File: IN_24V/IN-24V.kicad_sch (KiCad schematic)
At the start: 12 parts, among them U1 SN74LVC1T45DCK

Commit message: IN-24V
correction cartouche
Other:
- company: Style And Design -> (none)
- title: Module OUT 1 5V -> IN 24V
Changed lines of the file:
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@@
 	(paper "A4")
 	(title_block
-		(title "Module OUT 1 5V")
-		(date "2024-03-04")
-		(rev "00")
-		(company "Style And Design")
-		(comment 1 "T.ORLANDI")
+		(title "IN 24V")
+		(date "2024-12-03")
+		(rev "0")
 	)
 	(junction

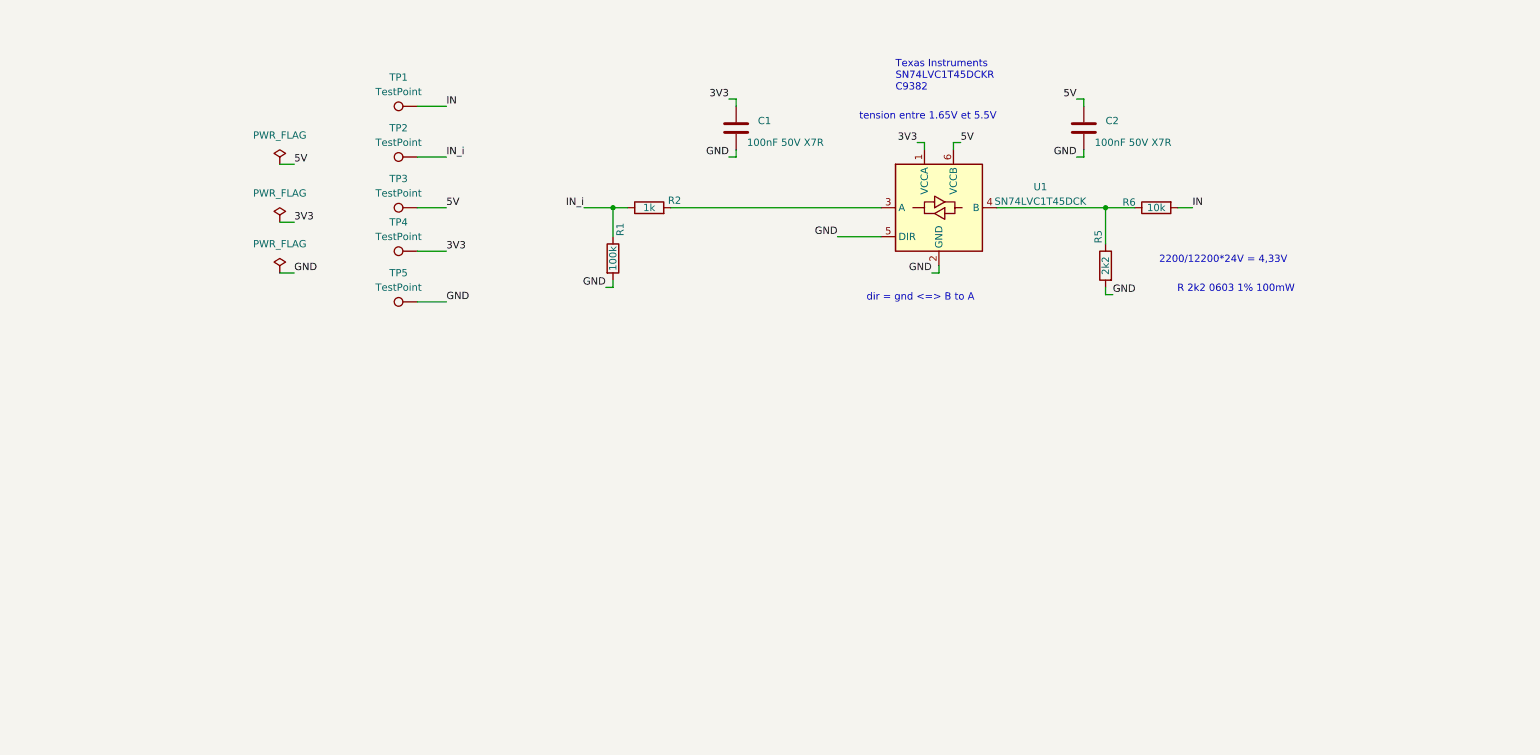
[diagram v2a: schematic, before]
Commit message: IN-24V passage à opto et nouveau format
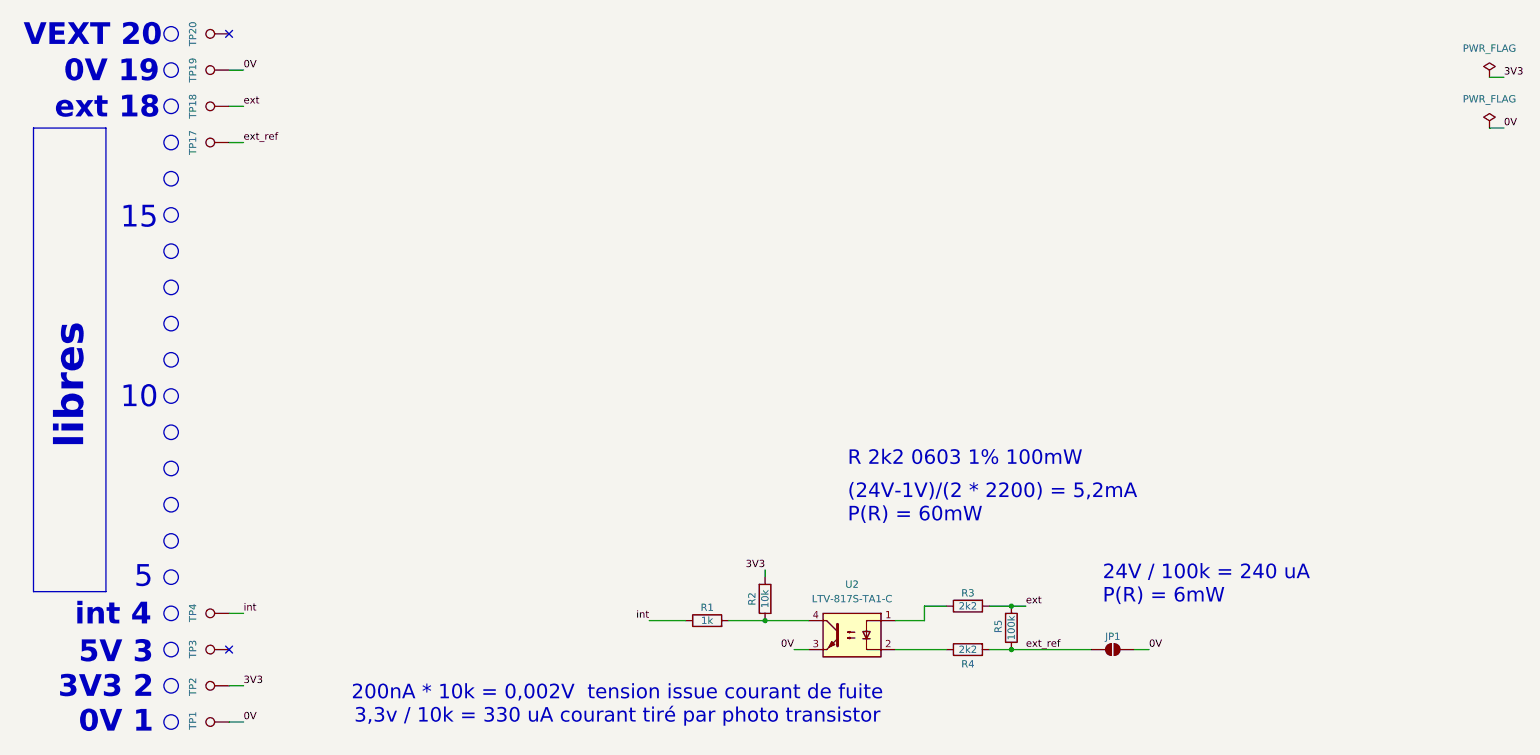
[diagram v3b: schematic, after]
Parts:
- removed C1, C2: 100nF 50V X7R, Capacitor_SMD:C_0603_1608Metric, symbol Device:C
- removed R6: 10k, Resistor_SMD:R_0603_1608Metric, symbol Device:R
- removed U1: SN74LVC1T45DCK, Package_TO_SOT_SMD:SOT-363_SC-70-6, symbol Logic_LevelTranslator:SN74LVC1T45DCK
- added JP1: SolderJumper_2_Open, Jumper:SolderJumper-2_P1.3mm_Open_TrianglePad1.0x1.5mm, symbol Jumper:SolderJumper_2_Open
- added R2: 10k, Resistor_SMD:R_0603_1608Metric, symbol Device:R
- added R4: 2k2, Resistor_SMD:R_0603_1608Metric, symbol Device:R
- added TP17, TP19, TP20: TestPoint, Chimere_comps:Pastille, symbol Connector:TestPoint
- added U2: LTV-817S-TA1-C, Package_DIP:SMDIP-4_W9.53mm, symbol Isolator:LTV-817S
- renumbered R2 to R1, R5 to R3, R1 to R5, TP5 to TP18
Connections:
- net 3V3: now also TP2.1, R2.2; no longer TP4.1
- net at R1.2: now also R2.1, U2.4
- net at R3.1: now also U2.1
- net 5V: no longer names the net of TP3.1
- net GND renamed ext
- net ext: now also R5.1; no longer R5.2
- net IN renamed 0V
- net 0V: now also JP1.2 (B), TP19.1, U2.3
- removed net IN_i: R1.1, R5.1, TP2.1
- new net: R4.1, U2.2
- new net ext_ref: JP1.1 (A), R4.2, R5.2, TP17.1
- new net int: R1.1, TP4.1
- no-connect marks 0 -> 2
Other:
- note added: "(24V-1V)/(2 * 2200) = 5,2mA P(R) = 60mW"
- note added: "0V 1"
- note added: "0V 19"
- note added: "10"
- note added: "15"
- note added: "200nA * 10k = 0,002V tension issue courant de fuite 3,3v / 10k = 330 uA courant tiré par photo transistor"
- note added: "24V / 100k = 240 uA P(R) = 6mW"
- note added: "3V3 2"
- note added: "5"
- note added: "5V 3"
- note added: "VEXT 20"
- note added: "ext 18"
- note added: "int 4"
- note added: "libres"
- note removed: "2200/12200*24V = 4,33V"
- note removed: "Texas Instruments SN74LVC1T45DCKR C9382"
- note removed: "dir = gnd <=> B to A"
- note removed: "tension entre 1.65V et 5.5V"
- moved on the sheet: R1, R3, R5, TP1, TP18, TP2, TP3, TP4
